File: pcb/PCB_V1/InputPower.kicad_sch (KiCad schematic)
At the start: 13 parts, among them U101 TPS54202DDCR

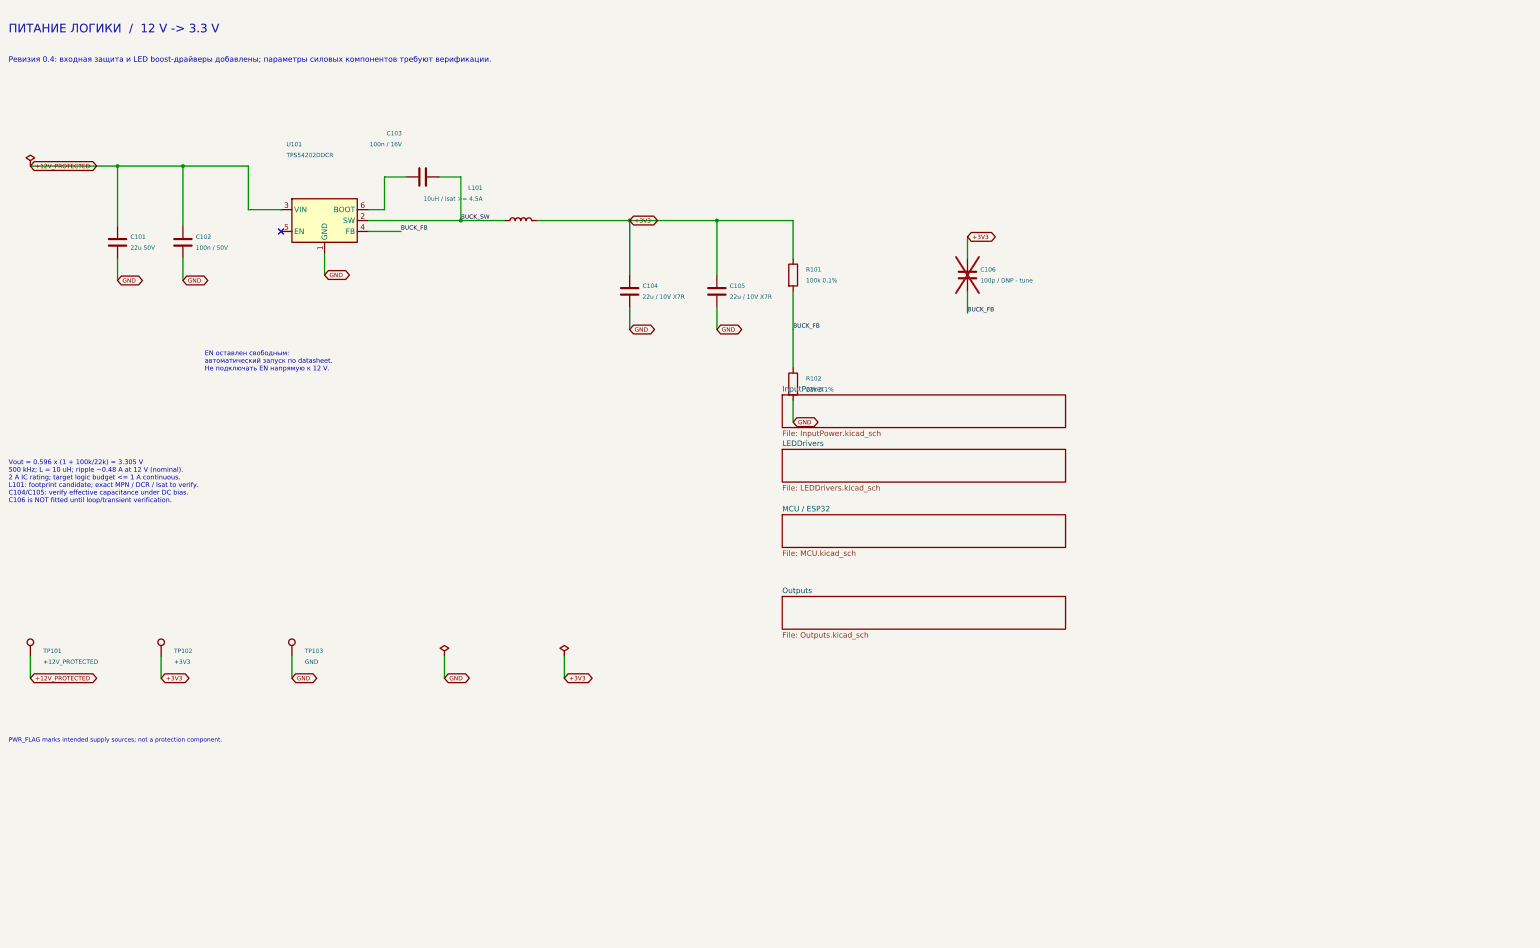
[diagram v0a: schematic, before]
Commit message: pcb: add protected input and independent LED boost drivers
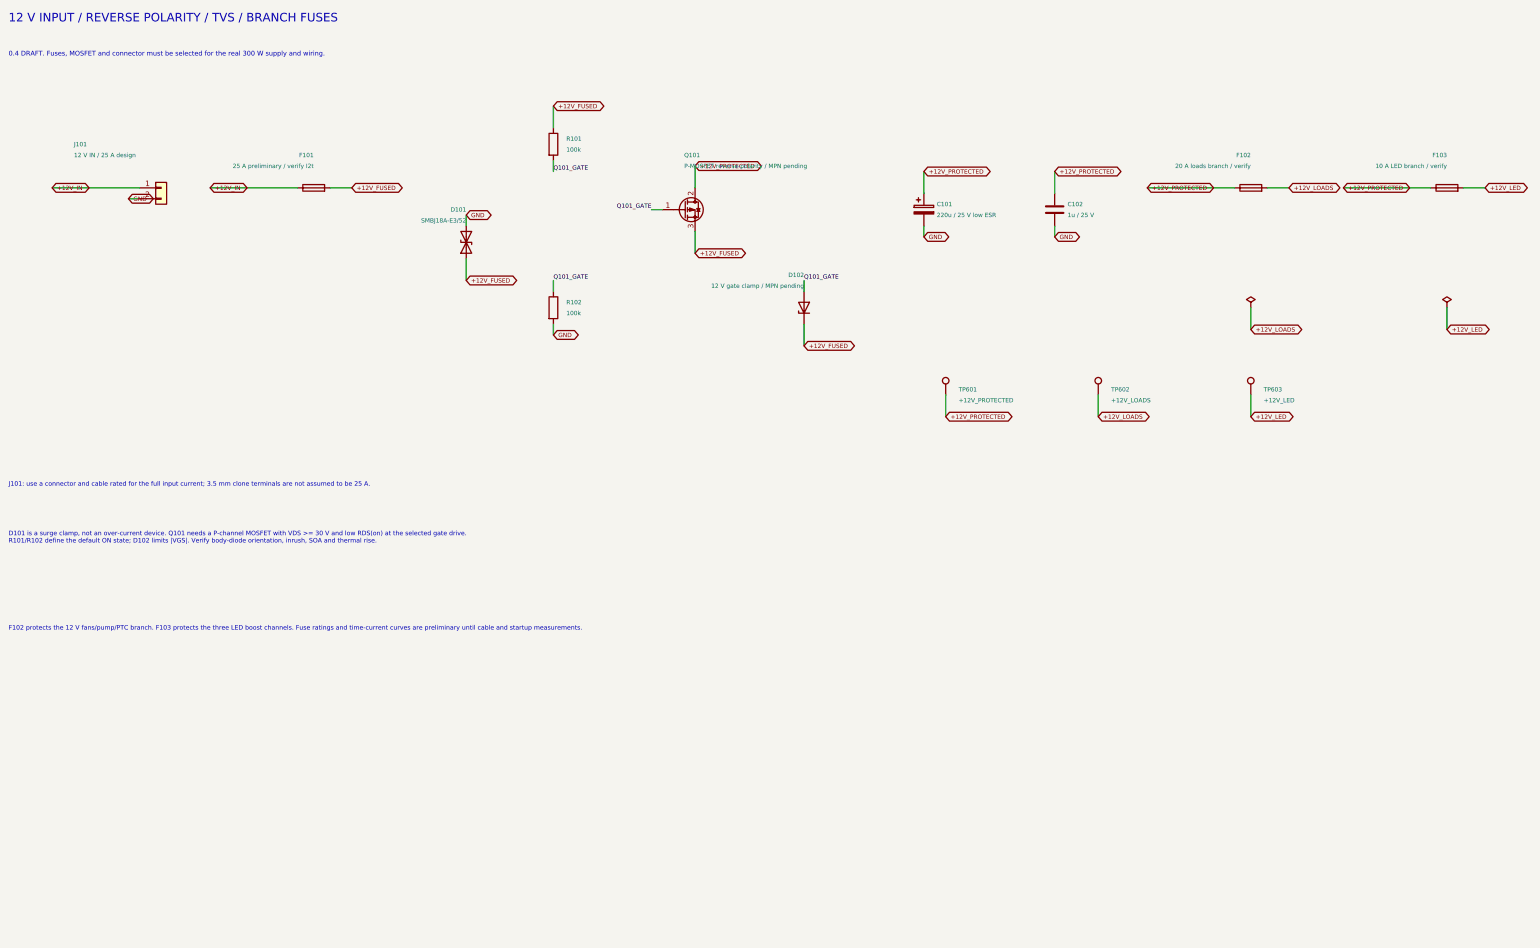
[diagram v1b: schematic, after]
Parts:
- removed C103: 100n / 16V, Capacitor_SMD:C_0603_1608Metric, symbol Device:C
- removed C104, C105: 22u / 10V X7R, Capacitor_SMD:C_0805_2012Metric, symbol Device:C
- removed C106: 100p / DNP - tune, Capacitor_SMD:C_0603_1608Metric, symbol Device:C
- removed L101: 10uH / Isat >= 4.5A, Inductor_SMD:L_Coilcraft_XAL7050-XXX, symbol Device:L
- removed TP101: +12V_PROTECTED, TestPoint:TestPoint_Pad_D2.0mm, symbol Connector:TestPoint
- removed TP102: +3V3, TestPoint:TestPoint_Pad_D2.0mm, symbol Connector:TestPoint
- removed TP103: GND, TestPoint:TestPoint_Pad_D2.0mm, symbol Connector:TestPoint
- removed U101: TPS54202DDCR, Package_TO_SOT_SMD:SOT-23-6, symbol Regulator_Switching:TPS54202DDC
- added D101: SMBJ18A-E3/52, Diode_SMD:D_SMB, symbol Device:D_TVS
- added D102: 12 V gate clamp / MPN pending, Diode_SMD:D_SOD-323, symbol Device:D_Zener
- added F101: 25 A preliminary / verify I2t, Fuse:Fuse_2920_7451Metric, symbol Device:Fuse
- added F102: 20 A loads branch / verify, Fuse:Fuse_2920_7451Metric, symbol Device:Fuse
- added F103: 10 A LED branch / verify, Fuse:Fuse_2920_7451Metric, symbol Device:Fuse
- added J101: 12 V IN / 25 A design, TerminalBlock_Phoenix:TerminalBlock_Phoenix_MKDS-1,5-2-5.08_1x02_P5.08mm_Horizontal, symbol Connector_Generic:Conn_01x02
- added Q101: P-MOSFET reverse-polarity / MPN pending, Package_SO:PowerPAK_SO-8L_Single, symbol Transistor_FET:Q_PMOS_GDS
- added TP601: +12V_PROTECTED, TestPoint:TestPoint_Pad_D2.0mm, symbol Connector:TestPoint
- added TP602: +12V_LOADS, TestPoint:TestPoint_Pad_D2.0mm, symbol Connector:TestPoint
- added TP603: +12V_LED, TestPoint:TestPoint_Pad_D2.0mm, symbol Connector:TestPoint
- C101: value 22u 50V -> 220u / 25 V low ESR; footprint Capacitor_SMD:C_1210_3225Metric -> Capacitor_SMD:CP_Elec_10x10.5; symbol Device:C -> Device:C_Polarized
- C102: value 100n / 50V -> 1u / 25 V; footprint Capacitor_SMD:C_0603_1608Metric -> Capacitor_SMD:C_1210_3225Metric
- R101: value 100k 0.1% -> 100k
- R102: value 22k 0.1% -> 100k
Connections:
- net +12V_PROTECTED: now also F102.1, F103.1, Q101.2 (D), TP601.1
- net GND: now also D101.2 (A2), J101.2 (Pin_2)
- net +3V3 renamed +12V_FUSED
- net +12V_FUSED: now also D101.1 (A1), D102.1 (K), F101.2, Q101.3 (S)
- net BUCK_FB renamed Q101_GATE
- net Q101_GATE: now also D102.2 (A), Q101.1 (G)
- new net +12V_IN: F101.1, J101.1 (Pin_1)
- new net +12V_LED: F103.2, TP603.1
- new net +12V_LOADS: F102.2, TP602.1
- no-connect marks 1 -> 0
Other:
- removed sheet InputPower
- removed sheet LEDDrivers
- removed sheet MCU / ESP32
- removed sheet Outputs
- note added: "0.4 DRAFT. Fuses, MOSFET and connector must be selected for the real 300 W supply and wiring."
- note added: "12 V INPUT / REVERSE POLARITY / TVS / BRANCH FUSES"
- note added: "D101 is a surge clamp, not an over-current device. Q101 needs a P-channel MOSFET with VDS >= 30 V and low RDS(on) at the selected gate drive. R101/R102 define the default ON state; D102 limits |VGS|. Verify body-diode orientation, inrush, SOA and thermal rise."
- note added: "F102 protects the 12 V fans/pump/PTC branch. F103 protects the three LED boost channels. Fuse ratings and time-current curves are preliminary until cable and startup measurements."
- note added: "J101: use a connector and cable rated for the full input current; 3.5 mm clone terminals are not assumed to be 25 A."
- note removed: "EN оставлен свободным: автоматический запуск по datasheet. Не подключать EN напрямую к 12 V."
- note removed: "PWR_FLAG marks intended supply sources; not a protection component."
- note removed: "Vout = 0.596 x (1 + 100k/22k) = 3.305 V 500 kHz; L = 10 uH; ripple ~0.48 A at 12 V (nominal). 2 A IC rating; target logic budget <= 1 A continuous. L101: footprint candidate; exact MPN / DCR / Isat to verify. C104/C105: verify effective capacitance under DC bias. C106 is NOT fitted until loop/transient verification."
- note removed: "ПИТАНИЕ ЛОГИКИ / 12 V -> 3.3 V"
- note removed: "Ревизия 0.4: входная защита и LED boost-драйверы добавлены; параметры силовых компонентов требуют верификации."
- title: 01 - Logic power / 12 V to 3.3 V -> 06 - 12 V input protection and branch fuses
- moved on the sheet: C102, R101, R102

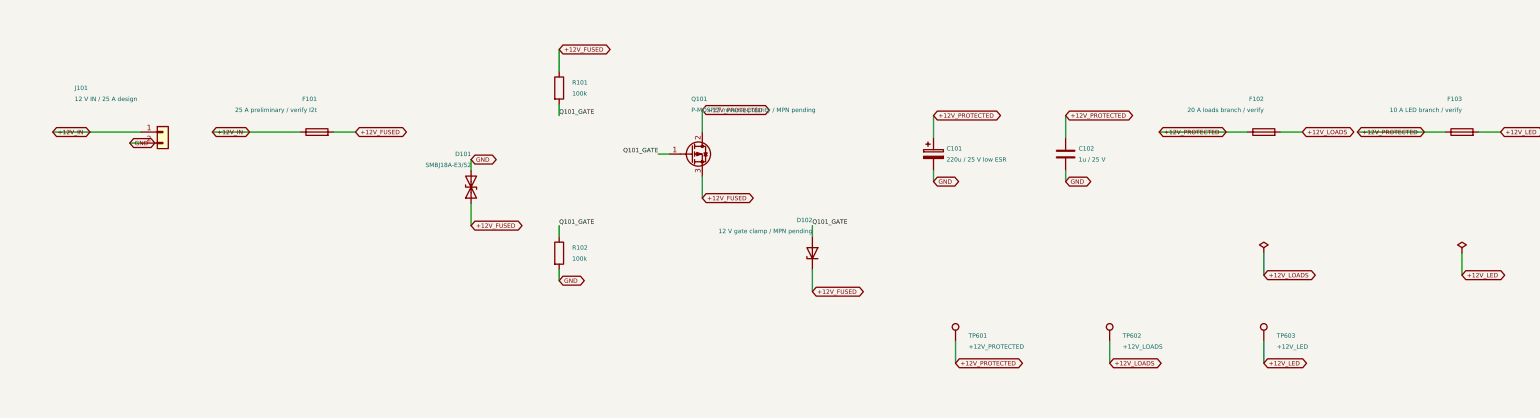
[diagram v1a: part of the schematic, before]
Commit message: pcb: make schematic references globally unique
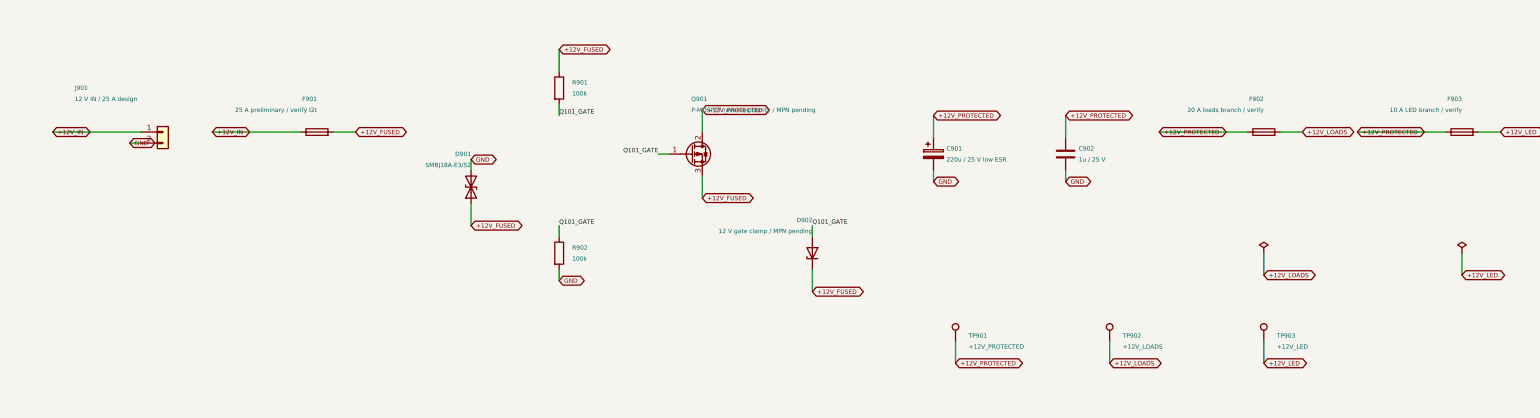
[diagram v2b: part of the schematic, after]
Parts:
- renumbered C101 to C901, C102 to C902, D101 to D901, D102 to D902, F101 to F901, F102 to F902, F103 to F903, J101 to J901, Q101 to Q901, R101 to R901, R102 to R902, TP601 to TP901, TP602 to TP902, TP603 to TP903
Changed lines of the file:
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@@
 		(in_pos_files yes)
 		(dnp no)
-		(property "Reference" "C101"
+		(property "Reference" "C901"
 			(at 236.68 59.69 0)
 			(show_name no)
@@
 			(project "PCB_V1"
 				(path "/7c30e6d8-4e60-4647-b4d3-d05e639d6467/13f6ec92-6d25-5cb3-b953-f0854e3d007b"
-					(reference "C101")
+					(reference "C901")
 					(unit 1)
 				)
@@
 		(in_pos_files yes)
 		(dnp no)
-		(property "Reference" "F103"
+		(property "Reference" "F903"
 			(at 355.6 48.26 90)
 			(show_name no)
@@
 			(project "PCB_V1"
 				(path "/7c30e6d8-4e60-4647-b4d3-d05e639d6467/13f6ec92-6d25-5cb3-b953-f0854e3d007b"
-					(reference "F103")
+					(reference "F903")
 					(unit 1)
 				)
@@
 		(in_pos_files yes)
 		(dnp no)
-		(property "Reference" "R101"
+		(property "Reference" "R901"
 			(at 150.32 44.45 0)
 			(show_name no)
@@
 			(project "PCB_V1"
 				(path "/7c30e6d8-4e60-4647-b4d3-d05e639d6467/13f6ec92-6d25-5cb3-b953-f0854e3d007b"
-					(reference "R101")
+					(reference "R901")
 					(unit 1)
 				)
@@
 		(in_pos_files yes)
 		(dnp no)
-		(property "Reference" "F102"
+		(property "Reference" "F902"
 			(at 309.88 48.26 90)
 			(show_name no)
@@
 			(project "PCB_V1"
 				(path "/7c30e6d8-4e60-4647-b4d3-d05e639d6467/13f6ec92-6d25-5cb3-b953-f0854e3d007b"
-					(reference "F102")
+					(reference "F902")
 					(unit 1)
 				)
@@
 		(in_pos_files yes)
 		(dnp no)
-		(property "Reference" "D101"
+		(property "Reference" "D901"
 			(at 127 60.96 90)
 			(show_name no)
@@
 			(project "PCB_V1"
 				(path "/7c30e6d8-4e60-4647-b4d3-d05e639d6467/13f6ec92-6d25-5cb3-b953-f0854e3d007b"
-					(reference "D101")
+					(reference "D901")
 					(unit 1)
 				)
@@
 		(in_pos_files yes)
 		(dnp no)
-		(property "Reference" "C102"
+		(property "Reference" "C902"
 			(at 267.16 59.69 0)
 			(show_name no)
@@
 			(project "PCB_V1"
 				(path "/7c30e6d8-4e60-4647-b4d3-d05e639d6467/13f6ec92-6d25-5cb3-b953-f0854e3d007b"
-					(reference "C102")
+					(reference "C902")
 					(unit 1)
 				)
@@
 		(in_pos_files yes)
 		(dnp no)
-		(property "Reference" "Q101"
+		(property "Reference" "Q901"
 			(at 177.8 48.26 0)
 			(show_name no)
@@
 			(project "PCB_V1"
 				(path "/7c30e6d8-4e60-4647-b4d3-d05e639d6467/13f6ec92-6d25-5cb3-b953-f0854e3d007b"
-					(reference "Q101")
+					(reference "Q901")
 					(unit 1)
 				)
@@
 		(in_pos_files yes)
 		(dnp no)
-		(property "Reference" "TP602"
+		(property "Reference" "TP902"
 			(at 277.32 102.87 0)
 			(show_name no)
@@
 			(project "PCB_V1"
 				(path "/7c30e6d8-4e60-4647-b4d3-d05e639d6467/13f6ec92-6d25-5cb3-b953-f0854e3d007b"
-					(reference "TP602")
+					(reference "TP902")
 					(unit 1)
 				)
@@
 		(in_pos_files yes)
 		(dnp no)
-		(property "Reference" "F101"
+		(property "Reference" "F901"
 			(at 91.44 48.26 90)
 			(show_name no)
@@
 			(project "PCB_V1"
 				(path "/7c30e6d8-4e60-4647-b4d3-d05e639d6467/13f6ec92-6d25-5cb3-b953-f0854e3d007b"
-					(reference "F101")
+					(reference "F901")
 					(unit 1)
 				)
@@
 		(in_pos_files yes)
 		(dnp no)
-		(property "Reference" "R102"
+		(property "Reference" "R902"
 			(at 150.32 82.55 0)
 			(show_name no)
@@
 			(project "PCB_V1"
 				(path "/7c30e6d8-4e60-4647-b4d3-d05e639d6467/13f6ec92-6d25-5cb3-b953-f0854e3d007b"
-					(reference "R102")
+					(reference "R902")
 					(unit 1)
 				)
@@
 		(in_pos_files yes)
 		(dnp no)
-		(property "Reference" "D102"
+		(property "Reference" "D902"
 			(at 205.74 76.2 90)
 			(show_name no)
@@
 			(project "PCB_V1"
 				(path "/7c30e6d8-4e60-4647-b4d3-d05e639d6467/13f6ec92-6d25-5cb3-b953-f0854e3d007b"
-					(reference "D102")
+					(reference "D902")
 					(unit 1)
 				)
@@
 		(in_pos_files yes)
 		(dnp no)
-		(property "Reference" "J101"
+		(property "Reference" "J901"
 			(at 35.56 45.72 0)
 			(show_name no)
@@
 			(project "PCB_V1"
 				(path "/7c30e6d8-4e60-4647-b4d3-d05e639d6467/13f6ec92-6d25-5cb3-b953-f0854e3d007b"
-					(reference "J101")
+					(reference "J901")
 					(unit 1)
 				)
@@
 		(in_pos_files yes)
 		(dnp no)
-		(property "Reference" "TP603"
+		(property "Reference" "TP903"
 			(at 312.88 102.87 0)
 			(show_name no)
@@
 			(project "PCB_V1"
 				(path "/7c30e6d8-4e60-4647-b4d3-d05e639d6467/13f6ec92-6d25-5cb3-b953-f0854e3d007b"
-					(reference "TP603")
+					(reference "TP903")
 					(unit 1)
 				)
@@
 		(in_pos_files yes)
 		(dnp no)
-		(property "Reference" "TP601"
+		(property "Reference" "TP901"
 			(at 241.76 102.87 0)
 			(show_name no)
@@
 			(project "PCB_V1"
 				(path "/7c30e6d8-4e60-4647-b4d3-d05e639d6467/13f6ec92-6d25-5cb3-b953-f0854e3d007b"
-					(reference "TP601")
-					(unit 1)
-				)
+					(reference "TP901")
+					(unit 1)
+				)
